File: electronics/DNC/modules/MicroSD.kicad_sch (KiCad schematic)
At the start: 5 parts

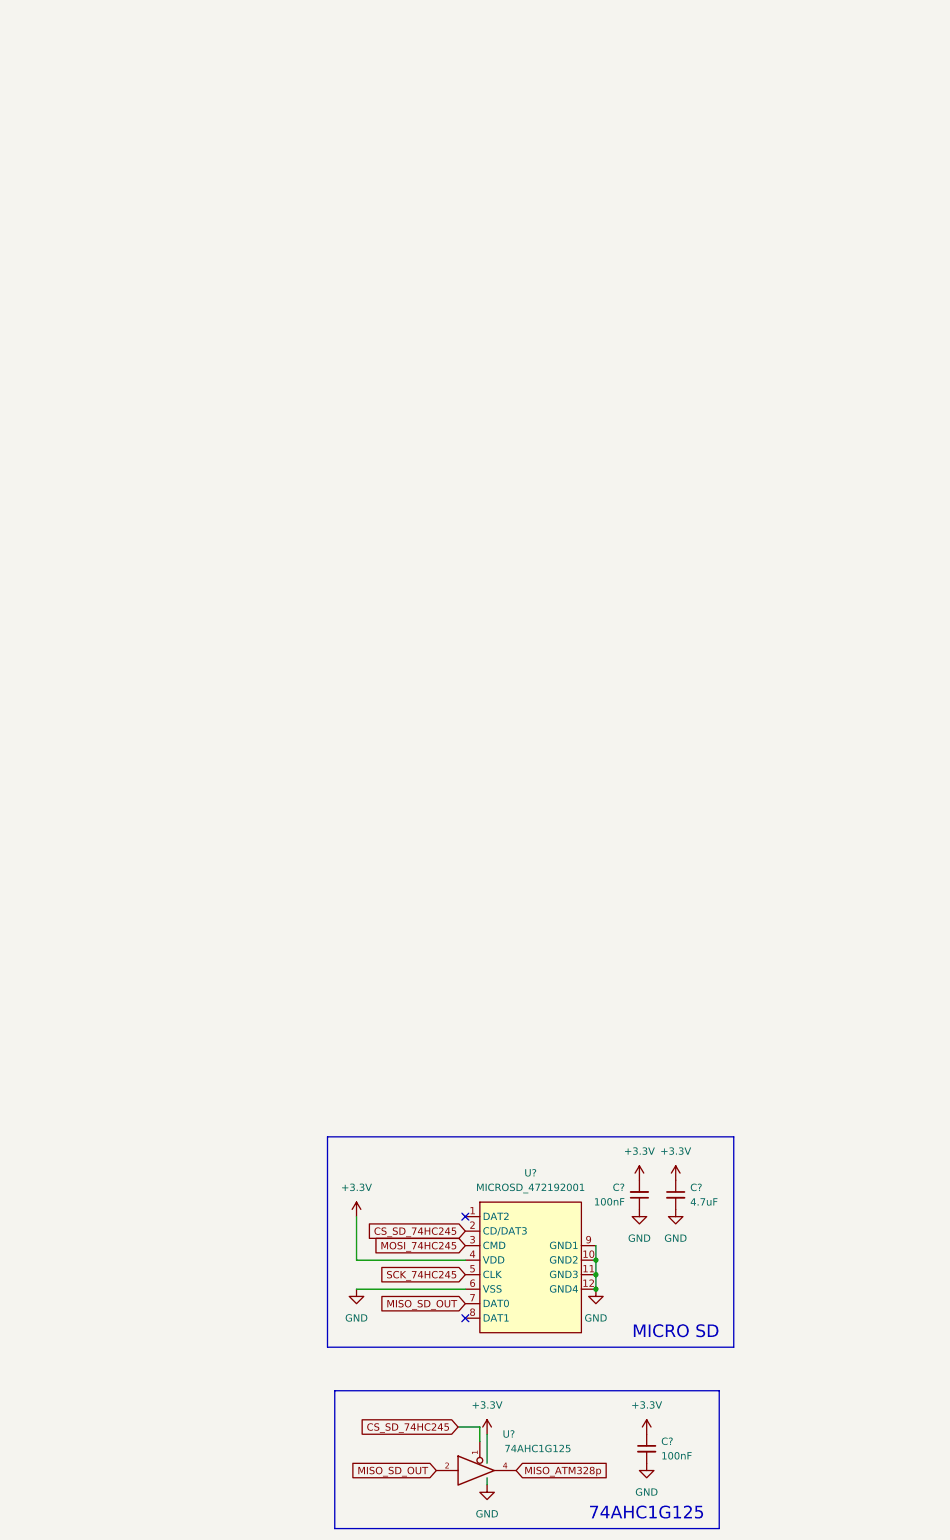
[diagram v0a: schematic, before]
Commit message: Se reemplazó la hoja del IMU por la de sensores y se agregó la hoja de indicadores
- Nueva hoja Sensores: IMU BMI270 (SPI1) y barómetro BMP581 (I2C1 propio, jumper BARO_ADDR).
- Nueva hoja Indicadores: buzzer piezo CPT-12123 con FDV303N y LEDs de estado en PB4/PB5.
- Se eliminó la hoja IMU.
- MicroSD por SDIO de 4 bits con filtro TPD6F002 y TVS ESD5Z3.3 en VDD.
- PMS: AP2112K en 3V3_SYS y LP5907 + ferrita en 3V3_SEN.
- Motores movidos a PA0-PA3 (TIM5) para liberar el SDIO.
- Arquitectura.drawio actualizado a la arquitectura v1 (ELRS por UART, sin OLED).
- Se agregó docs/RESUMEN_PROYECTO_DNC.md con decisiones y pendientes.

Co-Authored-By: Claude Opus 5.5 <noreply@anthropic.com>
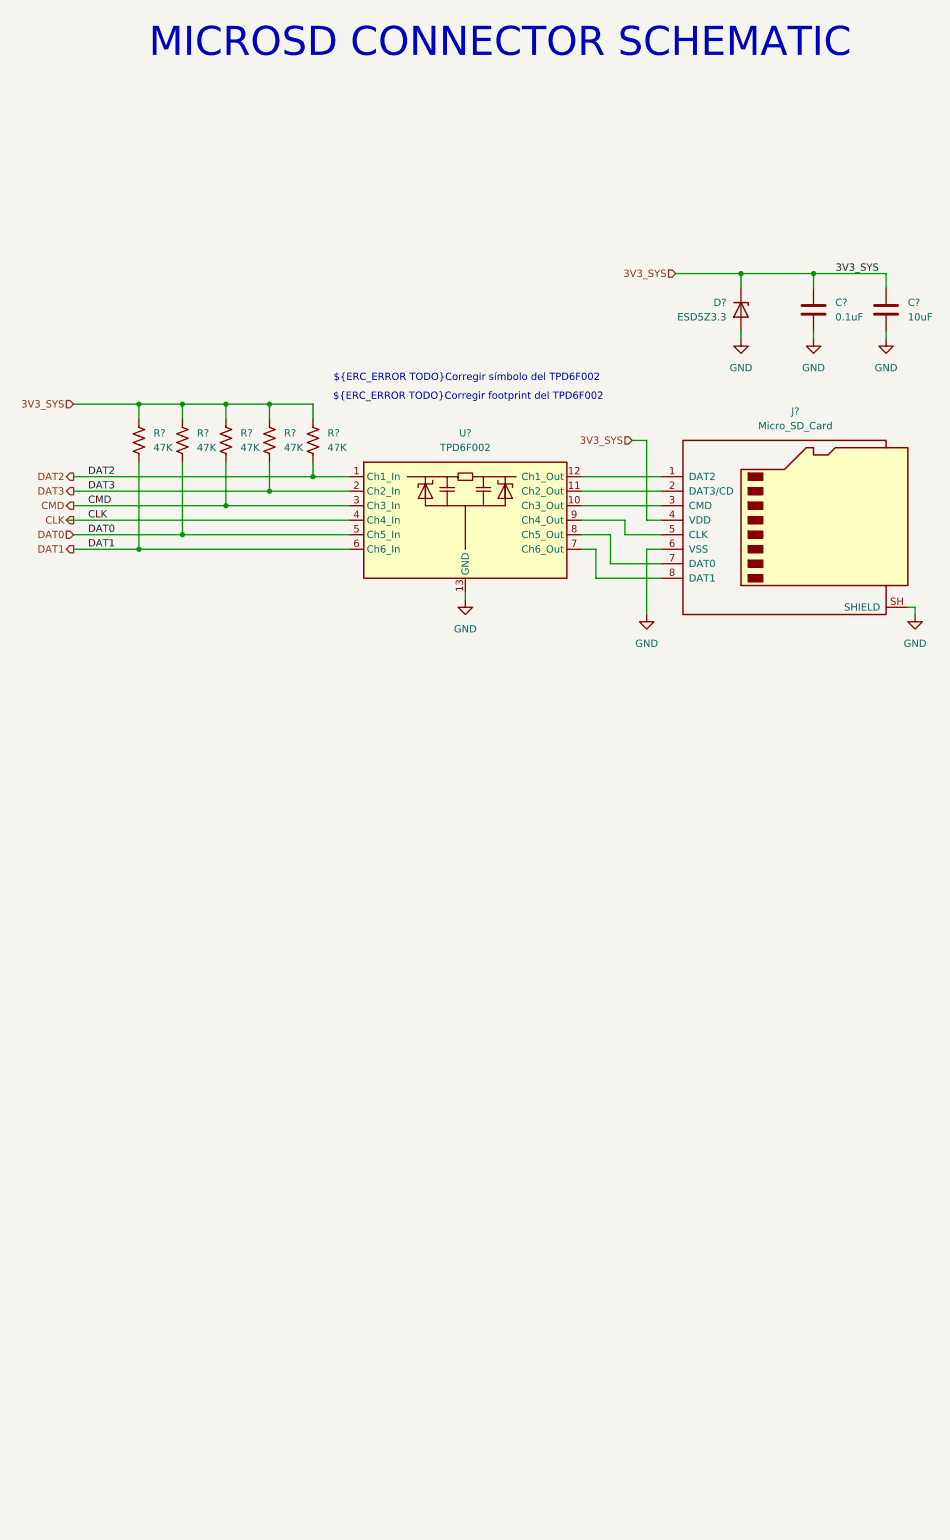
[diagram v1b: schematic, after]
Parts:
- removed C? (x2): 100nF, Capacitor_SMD:C_0402_1005Metric, symbol Device:C_Small
- removed C?: 4.7uF, Capacitor_SMD:C_0402_1005Metric, symbol Device:C_Small
- removed U?: MICROSD_472192001, Gen_devices:TF-SMD_472192001, symbol Gen_devices:MICROSD_472192001
- removed U?: 74AHC1G125, Package_TO_SOT_SMD:SOT-353_SC-70-5, symbol 74xGxx:74AHC1G125
- added C?: 10uF, symbol Device:C
- added C?: 0.1uF, symbol Device:C
- added D?: ESD5Z3.3, Diode_SMD:D_SOD-523, symbol Diode:ESD5Zxx
- added J?: Micro_SD_Card, Connector_Card:microSD_HC_Molex_47219-2001, symbol Connector:Micro_SD_Card
- added R? (x5): 47K, symbol Device:R_US
- added U?: TPD6F002, Package_SON:Texas_R-PWSON-N12_EP0.4x2mm, symbol Power_Protection:TPD6F003
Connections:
- net GND: now also C?.2, C?.2, D?.2 (A), J?.6 (VSS), J?.SH (SHIELD), U?.13 (GND)
- new net: J?.3 (CMD), U?.10 (Ch3_Out)
- new net: J?.2 (DAT3/CD), U?.11 (Ch2_Out)
- new net: J?.1 (DAT2), U?.12 (Ch1_Out)
- new net: J?.8 (DAT1), U?.7 (Ch6_Out)
- new net: J?.7 (DAT0), U?.8 (Ch5_Out)
- new net: J?.5 (CLK), U?.9 (Ch4_Out)
- new net 3V3_SYS: C?.1, C?.1, D?.1 (K), J?.4 (VDD), R?.1, R?.1, R?.1, R?.1, R?.1
- new net CLK: U?.4 (Ch4_In)
- new net CMD: R?.2, U?.3 (Ch3_In)
- new net DAT0: R?.2, U?.5 (Ch5_In)
- new net DAT1: R?.2, U?.6 (Ch6_In)
- new net DAT2: R?.2, U?.1 (Ch1_In)
- new net DAT3: R?.2, U?.2 (Ch2_In)
- no-connect marks 2 -> 0
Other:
- note added: "${ERC_ERROR TODO}Corregir footprint del TPD6F002"
- note added: "${ERC_ERROR TODO}Corregir símbolo del TPD6F002"
- note added: "MICROSD CONNECTOR SCHEMATIC"
- note removed: "74AHC1G125"
- note removed: "MICRO SD"
